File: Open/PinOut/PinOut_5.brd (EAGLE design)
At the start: 20 x 13 mm, 8 parts

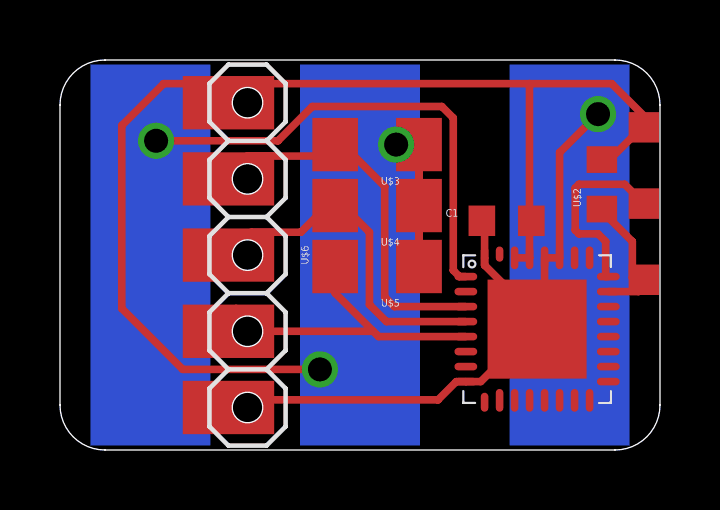
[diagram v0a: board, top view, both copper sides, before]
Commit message: Update Pinheader
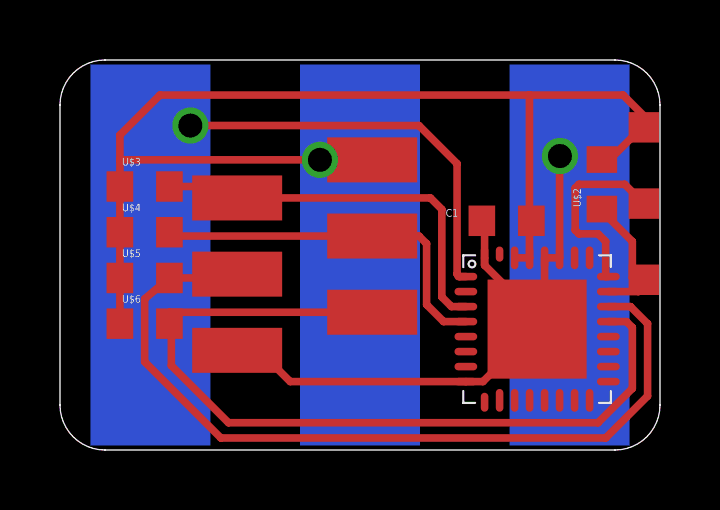
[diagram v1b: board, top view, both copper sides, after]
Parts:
- added U$7: PINHD_6MICROMATCH, thar:MICROMATCH6POL
- U$3, U$4, U$5: device thar:1206 -> thar:603
- U$6: value PINHD_52.54MOD -> 10k; device thar:PINHD_5_MOD -> thar:603
- moved U$3 7.87 mm to (4.57, 10.0), turned to 0 degrees
- moved U$4 7.80 mm to (4.57, 8.51), turned to 0 degrees
- moved U$5 7.76 mm to (4.57, 6.99), turned to 0 degrees
- moved U$6 4.12 mm to (4.57, 5.46), turned to 0 degrees
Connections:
- new net N$7: U$10.3, U$3.2, U$7.P$2
- net GND: now also U$7.P$6; no longer U$6.P$5
- net N$2: now also U$10.22, U$5.2, U$7.P$4; no longer U$10.3, U$3.2, U$6.P$2
- net N$5: now also U$10.21, U$6.2, U$7.P$5; no longer U$10.4, U$4.2, U$6.P$3
- net N$6: now also U$10.4, U$4.2, U$7.P$3; no longer U$10.5, U$5.2, U$6.P$4
- net VCC: now also U$6.1, U$7.P$1; no longer U$6.P$1
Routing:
- net N$5: track 12.0 -> 29.3 mm
- net N$2: track 13.0 -> 28.5 mm
- net N$7: track 0.00 -> 13.5 mm
- net VCC: track 63.6 -> 56.6 mm, vias 2 -> 1
- net GND: track 38.2 -> 33.8 mm
- net N$12: track 19.9 -> 17.9 mm
- net N$6: track 11.8 -> 12.4 mm
